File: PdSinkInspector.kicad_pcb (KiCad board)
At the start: 2 copper layers, 60 x 40 mm, 60 parts, among them IC2 STUSB4700YQTR, J1 USB_C_Receptacle, J2 USB_C_Receptacle, Q1 AO3401A, Q2 AO3401A, Q3 AO3401A, SW1 SW_MEC_5E, SW2 SW_MEC_5E, U1 RP2040, U2 W25Q128JVS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

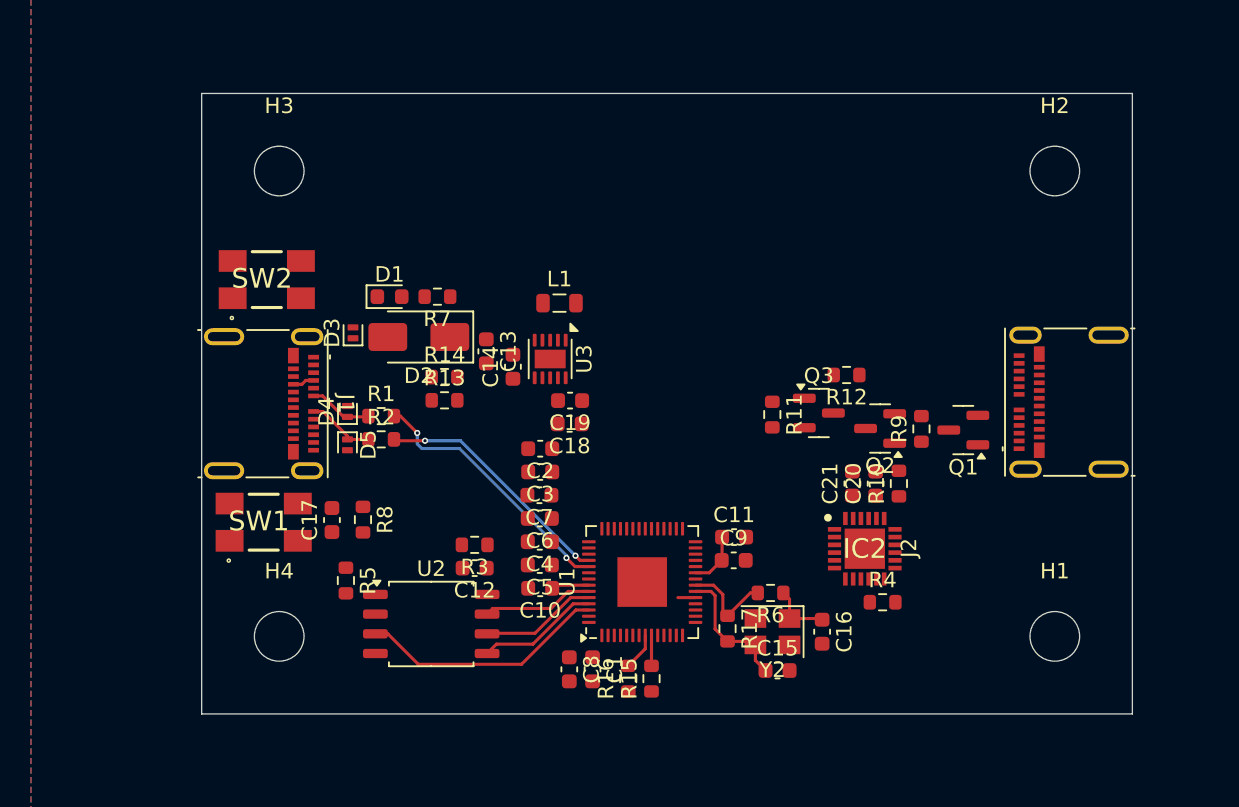
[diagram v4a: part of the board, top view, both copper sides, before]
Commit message: [Update]基板配線開始+チップを0402に変更
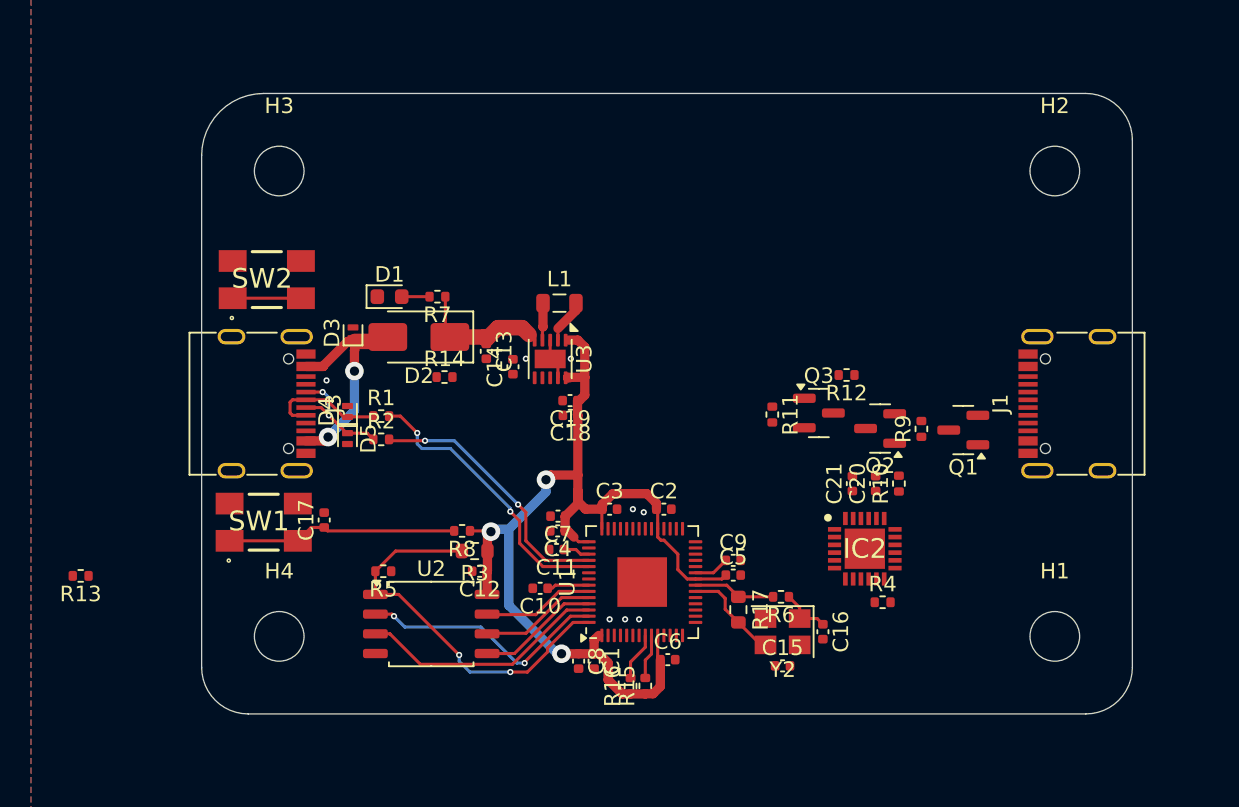
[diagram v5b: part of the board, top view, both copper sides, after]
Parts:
- removed J2: USB_C_Receptacle, Connector_USB:USB_C_Receptacle_Molex_105450-0101
- added J3: USB_C_Receptacle_USB2.0_16P, Connector_USB:USB_C_Receptacle_G-Switch_GT-USB-7010ASV, F.Cu at (103.0, 90.0)
- C1, C10, C11, C12, C13, C14, C15, C16, C17, C18, C19, C2, C20, C21, C3, C4, C5, C6, C7, C8, C9: footprint Capacitor_SMD:C_0603_1608Metric -> Capacitor_SMD:C_0402_1005Metric
- J1: value USB_C_Receptacle -> USB_C_Receptacle_USB2.0_16P; footprint Connector_USB:USB_C_Receptacle_Molex_105450-0101 -> Connector_USB:USB_C_Receptacle_G-Switch_GT-USB-7010ASV
- R1, R10, R11, R12, R13, R14, R15, R16, R2, R4, R5, R6, R7, R8, R9: footprint Resistor_SMD:R_0603_1608Metric -> Resistor_SMD:R_0402_1005Metric
- moved J1 53.0 mm to (157.0, 90.0), turned to 90 degrees
- moved R13 26.0 mm to (92.2, 101.1), turned to 180 degrees
- moved C5 12.5 mm to (134.3, 101.0), turned to 0 degrees
- moved C6 12.3 mm to (130.1, 106.5), turned to 0 degrees
- moved C11 11.5 mm to (122.9, 99.4), turned to 180 degrees
- moved C2 8.88 mm to (129.8, 96.8), turned to 0 degrees
- moved R8 6.43 mm to (116.8, 98.2), turned to 180 degrees
- moved C3 5.08 mm to (126.3, 96.8), turned to 0 degrees
- moved R5 2.48 mm to (111.7, 100.8), turned to 180 degrees
- moved C7 1.80 mm to (123.0, 97.2)
- moved R17 1.41 mm to (134.6, 103.3)
- moved C4 1.35 mm to (123.0, 98.2)
- moved C8 0.80 mm to (124.3, 106.6)
- moved R6 0.72 mm to (137.3, 102.5)
- moved Y2 0.65 mm to (137.4, 104.7)
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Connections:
- J1 pad A4: Net-(D2-A) -> Vout
- J1 pad A5: Net-(J1-CC1) -> Net-(IC2-CC1)
- J1 pad A6: USB_D+ -> unconnected-(J1-D+-PadA6)
- J1 pad A7: USB_D- -> unconnected-(J1-D--PadA7)
- J1 pad A9: Net-(D2-A) -> Vout
- J1 pad B4: Net-(D2-A) -> Vout
- J1 pad B5: Net-(J1-CC2) -> Net-(IC2-CC2)
- J1 pad B6: USB_D+ -> unconnected-(J1-D+-PadB6)
- J1 pad B7: USB_D- -> unconnected-(J1-D--PadB7)
- J1 pad B9: Net-(D2-A) -> Vout
- R13 pad 1: Net-(J1-CC2) -> Net-(J3-CC2)
- R14 pad 1: Net-(J1-CC1) -> Net-(J3-CC1)
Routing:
- net +3.3V: track 0.00 -> 69.9 mm, vias 0 -> 3
- net Net-(U1-QSPI_SS): track 0.00 -> 25.2 mm, vias 0 -> 2
- net Net-(U1-QSPI_SD1): track 0.00 -> 16.4 mm, vias 0 -> 2
- net RESET: track 0.00 -> 14.9 mm
- net Net-(D2-A): track 1.40 -> 14.5 mm, vias 0 -> 2
- net VBUS: track 0.00 -> 8.89 mm
- net BOOT: track 0.00 -> 4.40 mm
- net USB_D+: track 4.11 -> 7.68 mm
- net USB_D-: track 4.41 -> 7.96 mm, vias 0 -> 2
- net Net-(U3-L2): track 0.00 -> 2.87 mm
- net Net-(U3-L1): track 0.00 -> 2.41 mm
- net Net-(U1-XIN): track 8.48 -> 6.35 mm
- net Net-(D1-A): track 0.00 -> 1.79 mm
- net GND: track 1.14 -> 2.63 mm, vias 0 -> 8
- net Net-(U1-USB_DM): track 15.8 -> 17.2 mm
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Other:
- outline, holes or cut-outs redrawn

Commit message: 4/13進捗
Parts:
- added C22: 0.1u, Capacitor_SMD:C_0402_1005Metric, F.Cu at (118.8, 77.2)
- added C23: 0.1u, Capacitor_SMD:C_0402_1005Metric, F.Cu at (118.8, 78.2)
- added J2: Conn_01x12_Socket, Connector_FFC-FPC:Hirose_FH12-12S-0.5SH_1x12-1MP_P0.50mm_Horizontal, B.Cu at (140.2, 72.3)
- added R18: 10, Resistor_SMD:R_0402_1005Metric, F.Cu at (119.2, 75.1)
- added U4: FXMA108, Package_DFN_QFN:WQFN-20-1EP_2.5x4.5mm_P0.5mm_EP1x2.9mm, F.Cu at (122.8, 77.6)
- moved R13 19.2 mm to (108.8, 91.5), turned to 0 degrees
- moved C18 10.9 mm to (113.1, 93.0), turned to 90 degrees
- moved C19 10.2 mm to (114.0, 93.0), turned to 90 degrees
- moved R9 9.58 mm to (146.5, 101.2), turned to 0 degrees
- moved H2 9.22 mm to (157.0, 66.0)
- moved L1 9.18 mm to (120.3, 92.3), turned to -90 degrees
- moved H3 9.00 mm to (105.0, 66.0)
- moved R12 7.81 mm to (140.0, 95.8), turned to 0 degrees
- moved C21 7.52 mm to (141.1, 102.6)
- moved C20 7.47 mm to (143.7, 102.6)
- moved IC2 7.40 mm to (142.6, 106.8)
- moved Q2 7.40 mm to (143.5, 99.0)
- moved Q3 7.40 mm to (139.6, 98.0)
- moved R10 7.40 mm to (144.8, 102.5)
- moved U3 7.35 mm to (116.7, 91.7), turned to 180 degrees
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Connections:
- net I2C1_SCL renamed Net-(IC2-SCL)
- net I2C1_SDA renamed Net-(IC2-SDA)
- U1 pad 11: unconnected-(U1-GPIO8-Pad11) -> MISO
- U1 pad 12: unconnected-(U1-GPIO9-Pad12) -> SPI_CS
- U1 pad 13: unconnected-(U1-GPIO10-Pad13) -> SPI_SCK
- U1 pad 14: unconnected-(U1-GPIO11-Pad14) -> MOSI
- U1 pad 35: unconnected-(U1-GPIO23-Pad35) -> Data/Command
- U1 pad 36: unconnected-(U1-GPIO24-Pad36) -> LCD_RESET
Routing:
- net +3.3V: track 69.9 -> 123.2 mm, vias 3 -> 6
- net VBUS: track 8.89 -> 54.4 mm
- net MOSI: track 0.00 -> 32.6 mm, vias 0 -> 2
- net SPI_CS: track 0.00 -> 31.9 mm, vias 0 -> 2
- net SPI_SCK: track 0.00 -> 31.1 mm, vias 0 -> 2
- net Net-(J2-Pin_3): track 0.00 -> 25.1 mm, vias 0 -> 1
- net Net-(J2-Pin_7): track 0.00 -> 23.8 mm, vias 0 -> 1
- net Net-(IC2-CC2): track 0.00 -> 23.7 mm, vias 0 -> 2
- net Vout: track 0.00 -> 23.6 mm
- net Net-(J2-Pin_9): track 0.00 -> 23.1 mm, vias 0 -> 1
- net Net-(J2-Pin_8): track 0.00 -> 21.6 mm, vias 0 -> 1
- net Net-(J2-Pin_10): track 0.00 -> 21.5 mm, vias 0 -> 1
- net Data/Command: track 0.00 -> 21.2 mm, vias 0 -> 2
- net LCD_RESET: track 0.00 -> 21.1 mm, vias 0 -> 2
- net Net-(IC2-CC1): track 0.00 -> 20.9 mm, vias 0 -> 2
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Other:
- board size 60 x 40 mm -> 62 x 50 mm

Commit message: [Update]ガーバー作成
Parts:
- C1, C10, C12, C14, C17, C2, C22, C23, C3, C4, C5, C6, C7, C9: value 0.1u -> 0.1uF
- C11, C20, C21, C8: value 1u -> 1uF
- C13, C18, C19: value 10u -> 10uF
- C15, C16: value 27p -> 27pF
- L1: value 1.5u -> 1.5uH
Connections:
- SW2 pad 4: unconnected-(SW2-A-Pad4) -> GND
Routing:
- net GND: track 20.6 -> 22.5 mm, vias 74 -> 335
- net Net-(U1-USB_DM): track 16.5 -> 17.9 mm
- net Net-(U1-USB_DP): track 17.6 -> 18.7 mm
- net (no net): vias 0 -> 1
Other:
- board text added: "PD(Power Delibery) Sink Inspector"

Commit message: [Fix]不要なレベル変換を削除
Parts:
- removed C22, C23: 0.1uF, Capacitor_SMD:C_0402_1005Metric
- removed R18: 10, Resistor_SMD:R_0402_1005Metric
- removed U4: FXMA108, Package_DFN_QFN:WQFN-20-1EP_2.5x4.5mm_P0.5mm_EP1x2.9mm
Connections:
- J2 pad 10: Net-(J2-Pin_10) -> MOSI
- J2 pad 11: Net-(J2-Pin_11) -> LCD_RESET
- J2 pad 7: Net-(J2-Pin_7) -> Data/Command
- J2 pad 8: Net-(J2-Pin_8) -> SPI_CS
- J2 pad 9: Net-(J2-Pin_9) -> SPI_SCK
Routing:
- net Net-(J2-Pin_3): track 25.1 -> 0.00 mm, vias 1 -> 0
- net Net-(J2-Pin_7): track 23.8 -> 0.00 mm, vias 1 -> 0
- net Net-(J2-Pin_9): track 23.1 -> 0.00 mm, vias 1 -> 0
- net SPI_CS: track 31.9 -> 53.8 mm, vias 2 -> 1
- net Net-(J2-Pin_8): track 21.6 -> 0.00 mm, vias 1 -> 0
- net Net-(J2-Pin_10): track 21.5 -> 0.00 mm, vias 1 -> 0
- net LCD_RESET: track 21.1 -> 40.3 mm, vias 2 -> 1
- net Data/Command: track 21.2 -> 39.7 mm, vias 2 -> 3
- net Net-(J2-Pin_11): track 18.2 -> 0.00 mm, vias 1 -> 0
- net SPI_SCK: track 31.1 -> 48.8 mm, vias 2 -> 1
- net MOSI: track 32.6 -> 47.0 mm, vias 2 -> 3
- net GND: track 22.5 -> 17.2 mm, vias 335 -> 624
- net +3.3V: track 123.2 -> 119.2 mm, vias 6 -> 4
- net (no net): vias 1 -> 0
